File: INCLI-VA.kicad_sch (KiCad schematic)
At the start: 0 parts

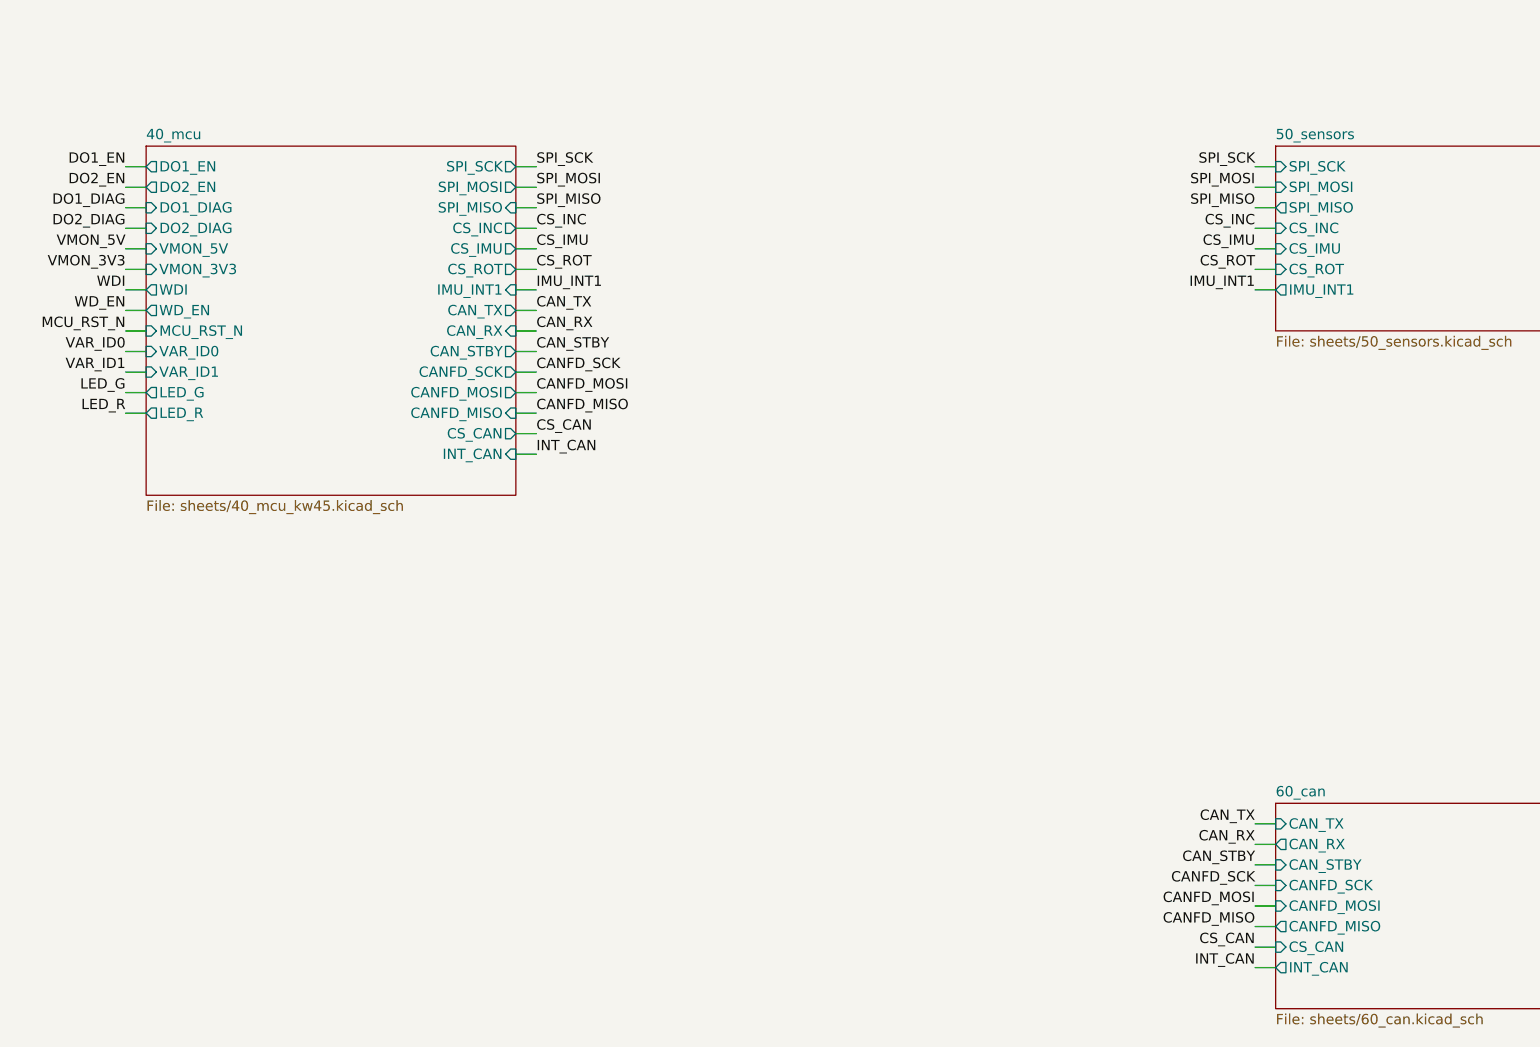
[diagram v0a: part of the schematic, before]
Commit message: Corrige la base del esquemático y añade reglas de proyecto
- Extrae el símbolo ADM3055E a lib/antmicro_adm3055ebriz.kicad_sym y lo
  registra en sym-lib-table con ${KIPRJMOD}.
- U1: huella Package_SO:SOIC-20W_7.5x12.8mm_P1.27mm (nota: verificar
  land pattern contra el datasheet).
- 10_power_input: power:GND -> GND_VEH; huellas y MPN de C1, C2 (0805
  X7R 100 V automotriz), C3 (EEE-HA2A470UP, 10x10) y F1 (1812, MPN
  pendiente).
- Nuevos pines jerárquicos CAN_SILENT (40_mcu -> 60_can, pull-down R1
  10k a GND_ISO) e IMU_INT2 (50_sensors -> 40_mcu).
- CLAUDE.md con reglas de librerías, campos, conexiones entre hojas,
  verificación por hoja y versión prototipo.
- Ignora output/ (reportes generados por kicad-mcp).

Co-Authored-By: Claude Opus 5.5 <noreply@anthropic.com>
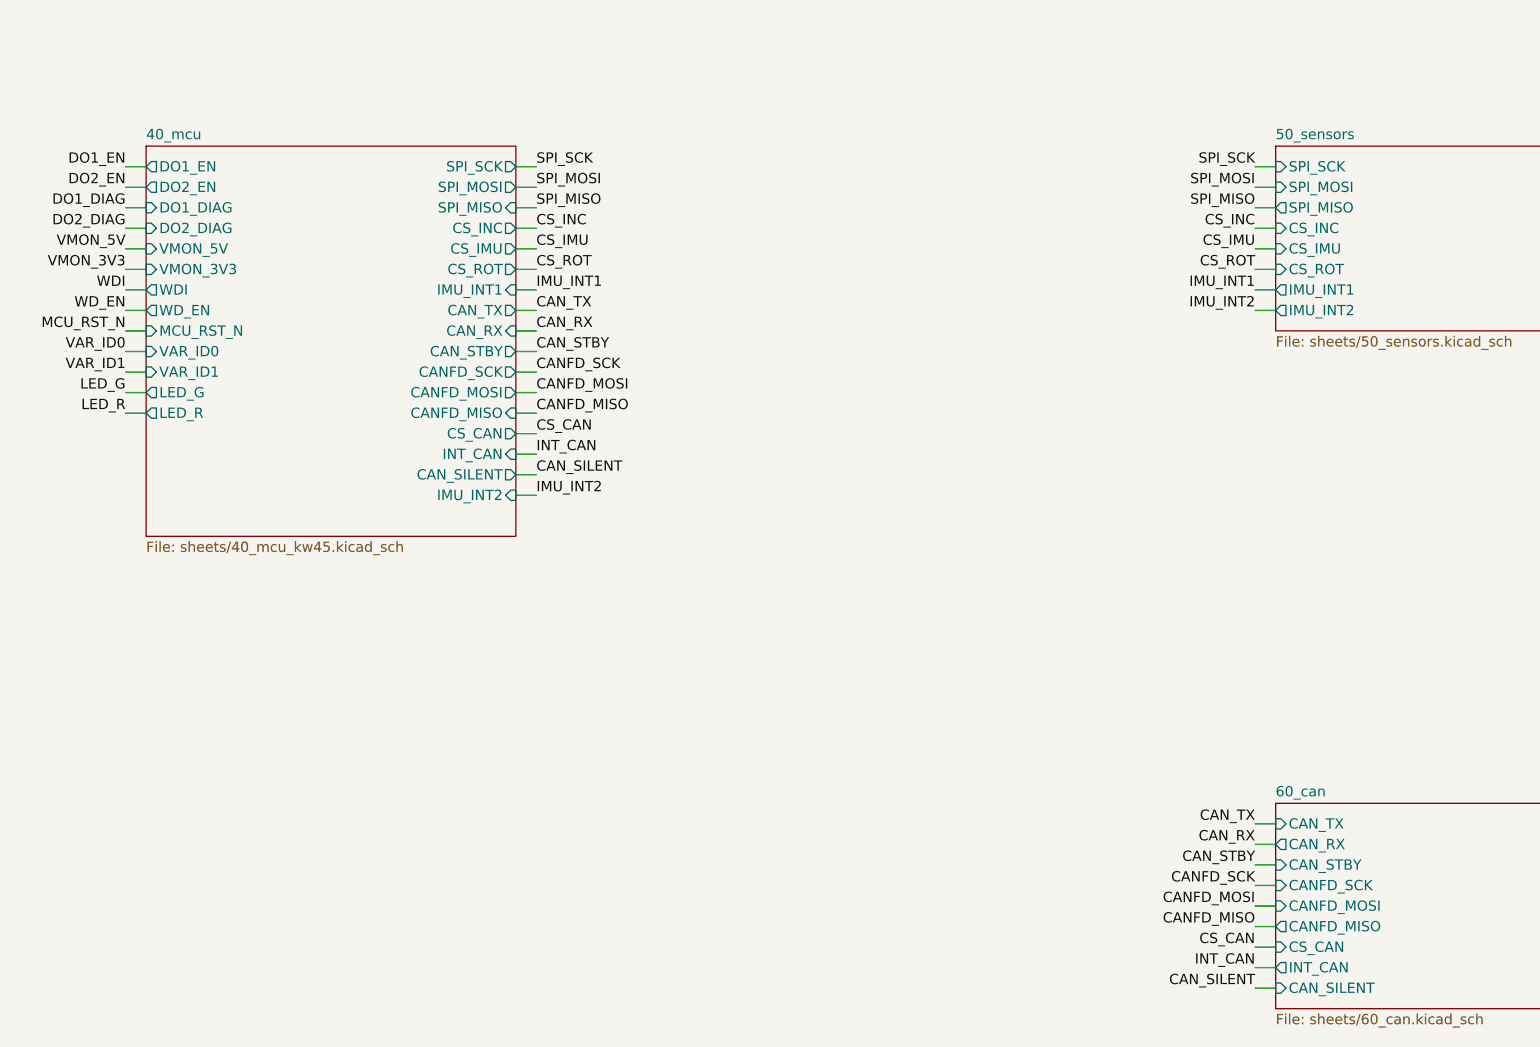
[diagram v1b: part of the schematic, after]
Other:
- sheet 40_mcu ports: added CAN_SILENT, IMU_INT2; removed none
- sheet 50_sensors ports: added IMU_INT2; removed none
- sheet 60_can ports: added CAN_SILENT; removed none
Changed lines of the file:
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@@
+			)
+		)
+		(pin "CAN_SILENT" input
+			(at 297.18 228.6 180)
+			(effects
+				(font
+					(size 1.27 1.27)
+				)
+				(justify left)
 			)
 		)
@@
 			)
 		)
+		(pin "IMU_INT2" output
+			(at 297.18 144.78 180)
+			(effects
+				(font
+					(size 1.27 1.27)
+				)
+				(justify left)
+			)
+		)
 		(instances
 			(project "INCLI-VA"
@@
 	(sheet
 		(at 157.48 124.46)
-		(size 45.72 43.18)
+		(size 45.72 48.26)
 		(exclude_from_sim no)
 		(in_bom yes)
@@
 		)
 		(property "Sheetfile" "sheets/40_mcu_kw45.kicad_sch"
-			(at 157.48 168.23 0)
+			(at 157.48 173.31 0)
 			(show_name no)
 			(do_not_autoplace no)
@@
 		(pin "INT_CAN" input
 			(at 203.2 162.56 0)
+			(effects
+				(font
+					(size 1.27 1.27)
+				)
+				(justify right)
+			)
+		)
+		(pin "CAN_SILENT" output
+			(at 203.2 165.1 0)
+			(effects
+				(font
+					(size 1.27 1.27)
+				)
+				(justify right)
+			)
+		)
+		(pin "IMU_INT2" input
+			(at 203.2 167.64 0)
 			(effects
 				(font
@@
 		)
 	)
+	(wire
+		(pts
+			(xy 203.2 165.1) (xy 205.74 165.1)
+		)
+		(stroke
+			(width 0)
+			(type default)
+		)
+	)
+	(label "CAN_SILENT"
+		(at 205.74 165.1 0)
+		(effects
+			(font
+				(size 1.27 1.27)
+			)
+			(justify left bottom)
+		)
+	)
+	(wire
+		(pts
+			(xy 203.2 167.64) (xy 205.74 167.64)
+		)
+		(stroke
+			(width 0)
+			(type default)
+		)
+	)
+	(label "IMU_INT2"
+		(at 205.74 167.64 0)
+		(effects
+			(font
+				(size 1.27 1.27)
+			)
+			(justify left bottom)
+		)
+	)
+	(wire
+		(pts
+			(xy 297.18 228.6) (xy 294.64 228.6)
+		)
+		(stroke
+			(width 0)
+			(type default)
+		)
+	)
+	(label "CAN_SILENT"
+		(at 294.64 228.6 180)
+		(effects
+			(font
+				(size 1.27 1.27)
+			)
+			(justify right bottom)
+		)
+	)
+	(wire
+		(pts
+			(xy 297.18 144.78) (xy 294.64 144.78)
+		)
+		(stroke
+			(width 0)
+			(type default)
+		)
+	)
+	(label "IMU_INT2"
+		(at 294.64 144.78 180)
+		(effects
+			(font
+				(size 1.27 1.27)
+			)
+			(justify right bottom)
+		)
+	)

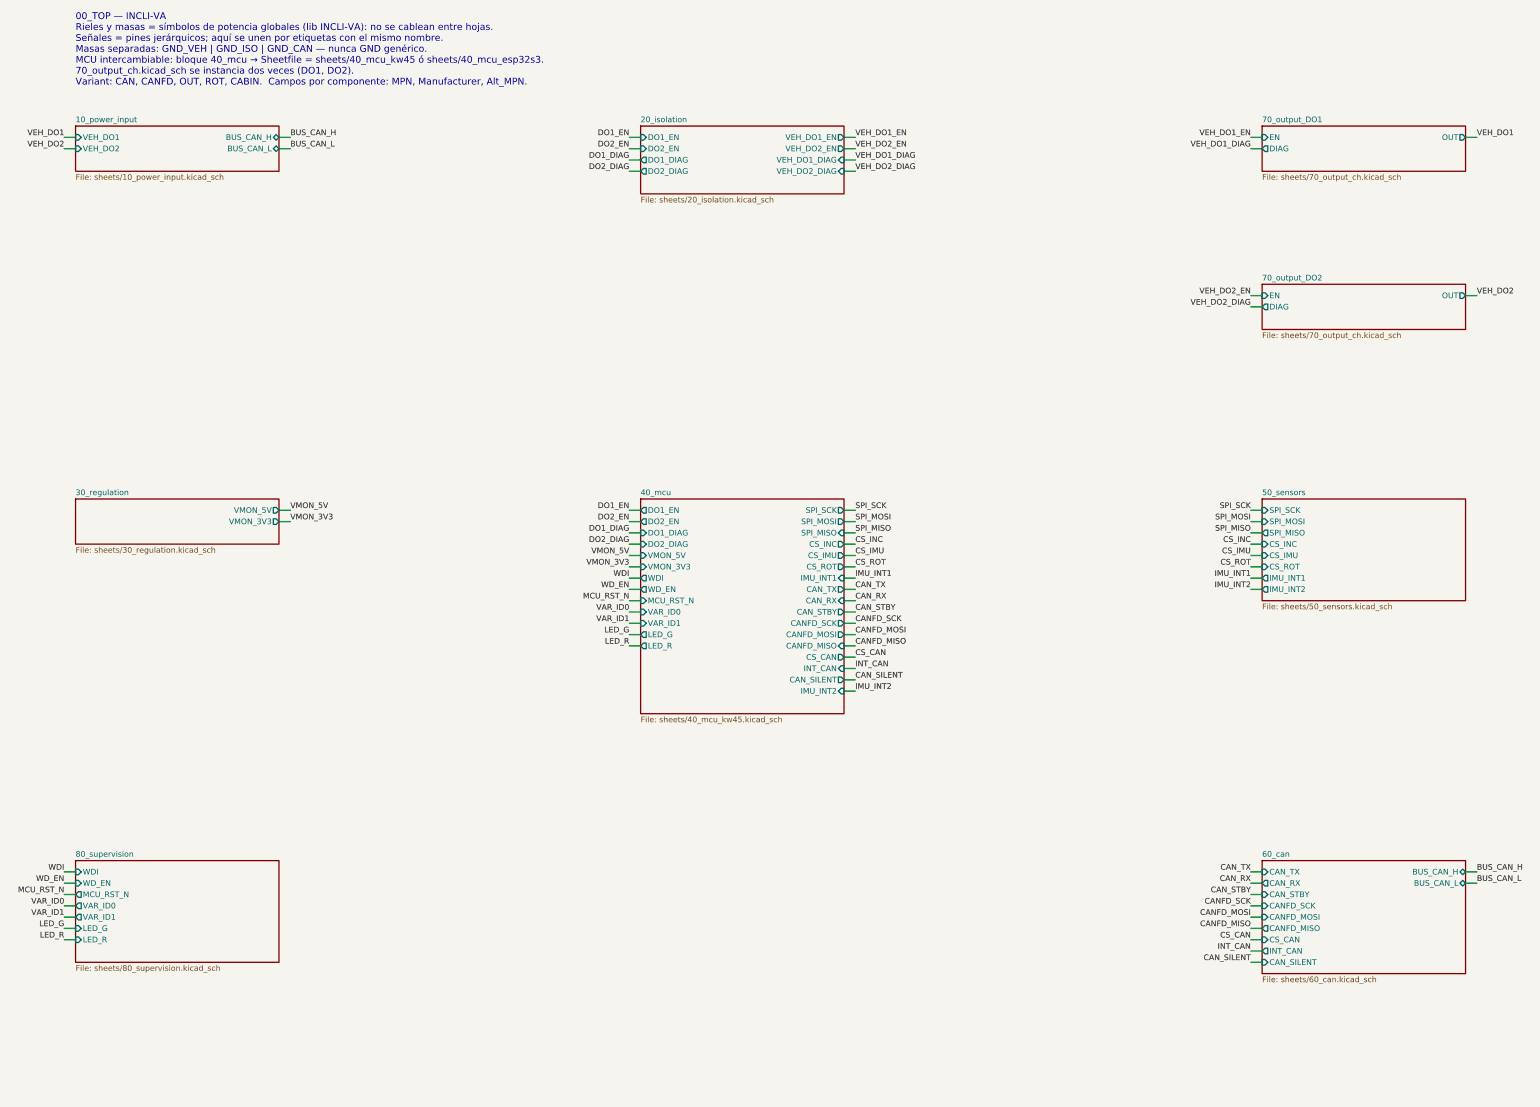
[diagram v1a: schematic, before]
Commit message: 70_output: salida low-side con latch y señal PWR_FLT
- 70_output (DO1/DO2): MOSFET FDD7N25LZ (demo, 250 V) con TVS SMCJ188A
  en el drenador, latch de sobrecorriente a ~0.7 A (R 1 ohm + BC817/BC807,
  rearme con EN=0), apagado del gate por PWR_FLT_N o latch (BAT54A) y
  DIAG por divisor del drenador con zener 5V1. OUT pasa a pasivo.
- Jerarquía: VEH_PWR_FLT_N de 10_power_input a 70_output y 20_isolation;
  PWR_FLT de 20_isolation a 40_mcu (KW45 y ESP32-S3).
- 10_power_input: solo interfaz (VEH_DO1/2 pasivos, VEH_PWR_FLT_N);
  el circuito con LM74930 va en un commit aparte.
- CLAUDE.md: procedimiento para componentes fuera de las librerías.
- README: 70_output es low-side.

Co-Authored-By: Claude Opus 5.5 <noreply@anthropic.com>
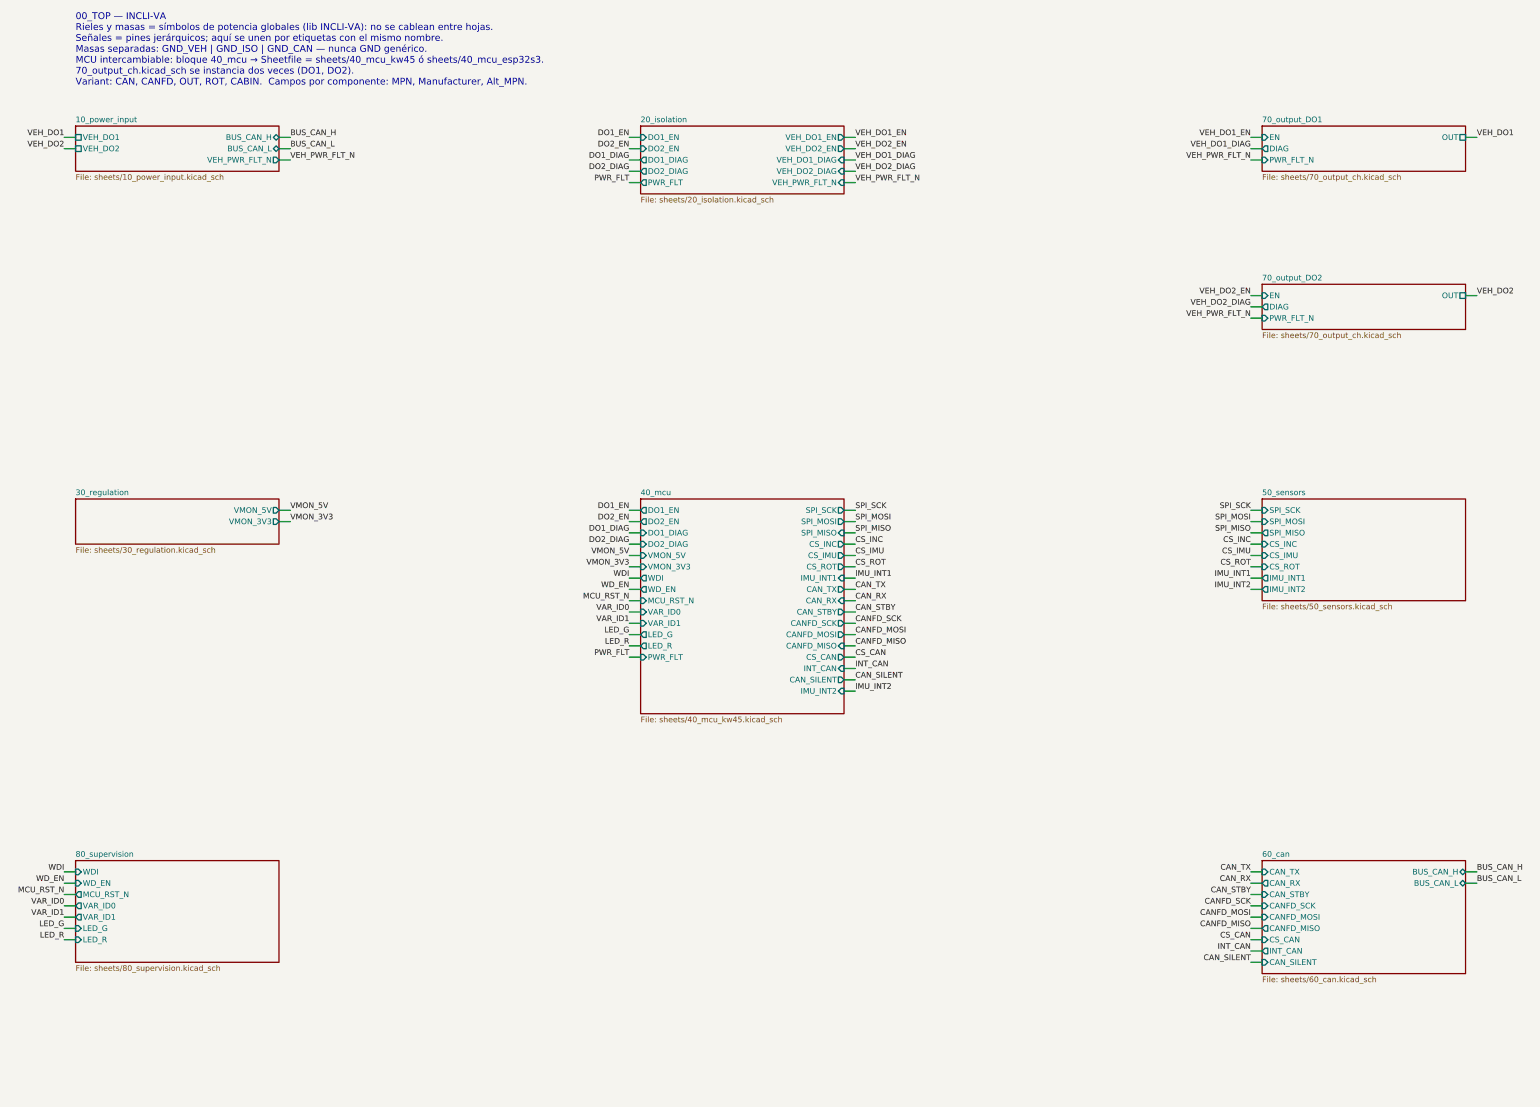
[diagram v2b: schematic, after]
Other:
- sheet 10_power_input ports: added VEH_PWR_FLT_N; removed none
- sheet 20_isolation ports: added PWR_FLT, VEH_PWR_FLT_N; removed none
- sheet 40_mcu ports: added PWR_FLT; removed none
- sheet 70_output_DO1 ports: added PWR_FLT_N; removed none
- sheet 70_output_DO2 ports: added PWR_FLT_N; removed none
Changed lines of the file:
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@@
 			)
 		)
-		(pin "VEH_DO1" input
+		(pin "VEH_DO1" passive
 			(at 30.48 43.18 180)
 			(effects
@@
 			)
 		)
-		(pin "VEH_DO2" input
+		(pin "VEH_DO2" passive
 			(at 30.48 45.72 180)
 			(effects
@@
 		(pin "BUS_CAN_L" bidirectional
 			(at 76.2 45.72 0)
+			(effects
+				(font
+					(size 1.27 1.27)
+				)
+				(justify right)
+			)
+		)
+		(pin "VEH_PWR_FLT_N" output
+			(at 76.2 48.26 0)
 			(effects
 				(font
@@
 			)
 		)
+		(pin "VEH_PWR_FLT_N" input
+			(at 203.2 53.34 0)
+			(effects
+				(font
+					(size 1.27 1.27)
+				)
+				(justify right)
+			)
+		)
+		(pin "PWR_FLT" output
+			(at 157.48 53.34 180)
+			(effects
+				(font
+					(size 1.27 1.27)
+				)
+				(justify left)
+			)
+		)
 		(instances
 			(project "INCLI-VA"
@@
 			)
 		)
+		(pin "PWR_FLT" input
+			(at 157.48 160.02 180)
+			(effects
+				(font
+					(size 1.27 1.27)
+				)
+				(justify left)
+			)
+		)
 		(instances
 			(project "INCLI-VA"
@@
 			)
 		)
-		(pin "OUT" output
+		(pin "OUT" passive
 			(at 342.9 78.74 0)
 			(effects
@@
 				)
 				(justify right)
+			)
+		)
+		(pin "PWR_FLT_N" input
+			(at 297.18 83.82 180)
+			(effects
+				(font
+					(size 1.27 1.27)
+				)
+				(justify left)
 			)
 		)
@@
 			)
 		)
-		(pin "OUT" output
+		(pin "OUT" passive
 			(at 342.9 43.18 0)
 			(effects
@@
 				)
 				(justify right)
+			)
+		)
+		(pin "PWR_FLT_N" input
+			(at 297.18 48.26 180)
+			(effects
+				(font
+					(size 1.27 1.27)
+				)
+				(justify left)
 			)
 		)
@@
 		(effects
 			(font
+				(size 1.27 1.27)
+			)
+			(justify right bottom)
+		)
+	)
+	(wire
+		(pts
+			(xy 76.2 48.26) (xy 78.74 48.26)
+		)
+		(stroke
+			(width 0)
+			(type default)
+		)
+	)
+	(label "VEH_PWR_FLT_N"
+		(at 78.74 48.26 0)
+		(effects
+			(font
+				(size 1.27 1.27)
+			)
+			(justify left bottom)
+		)
+	)
+	(wire
+		(pts
+			(xy 203.2 53.34) (xy 205.74 53.34)
+		)
+		(stroke
+			(width 0)
+			(type default)
+		)
+	)
+	(label "VEH_PWR_FLT_N"
+		(at 205.74 53.34 0)
+		(effects
+			(font
+				(size 1.27 1.27)
+			)
+			(justify left bottom)
+		)
+	)
+	(wire
+		(pts
+			(xy 157.48 53.34) (xy 154.94 53.34)
+		)
+		(stroke
+			(width 0)
+			(type default)
+		)
+	)
+	(label "PWR_FLT"
+		(at 154.94 53.34 180)
+		(effects
+			(font
+				(size 1.27 1.27)
+			)
+			(justify right bottom)
+		)
+	)
+	(wire
+		(pts
+			(xy 157.48 160.02) (xy 154.94 160.02)
+		)
+		(stroke
+			(width 0)
+			(type default)
+		)
+	)
+	(label "PWR_FLT"
+		(at 154.94 160.02 180)
+		(effects
+			(font
+				(size 1.27 1.27)
+			)
+			(justify right bottom)
+		)
+	)
+	(wire
+		(pts
+			(xy 297.18 48.26) (xy 294.64 48.26)
+		)
+		(stroke
+			(width 0)
+			(type default)
+		)
+	)
+	(label "VEH_PWR_FLT_N"
+		(at 294.64 48.26 180)
+		(effects
+			(font
+				(size 1.27 1.27)
+			)
+			(justify right bottom)
+		)
+	)
+	(wire
+		(pts
+			(xy 297.18 83.82) (xy 294.64 83.82)
+		)
+		(stroke
+			(width 0)
+			(type default)
+		)
+	)
+	(label "VEH_PWR_FLT_N"
+		(at 294.64 83.82 180)
+		(effects
+			(font
